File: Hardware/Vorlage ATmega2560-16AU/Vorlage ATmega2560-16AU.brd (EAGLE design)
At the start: 160 x 100 mm, 152 parts, among them IC1 CD74HC14PW, IC2 ATMEGA2560640V-8AU, IC3 SS39E, IC4 SS39E, IC5 74AC138D, IC6 XC6210B332MR, Q1 16MHz, Q10 PMV27UPER, Q2 32.768kHz, Q3 PMV27UPER, Q4 PMV27UPER, Q5 PMV27UPER, Q6 PMV27UPER, Q7 PMV27UPER, Q8 PMV27UPER, Q9 PMV27UPER, U1 LM35DZ, X1 2510-, X2 +5V, X3 2514-, X4 2510-, X5 2510-

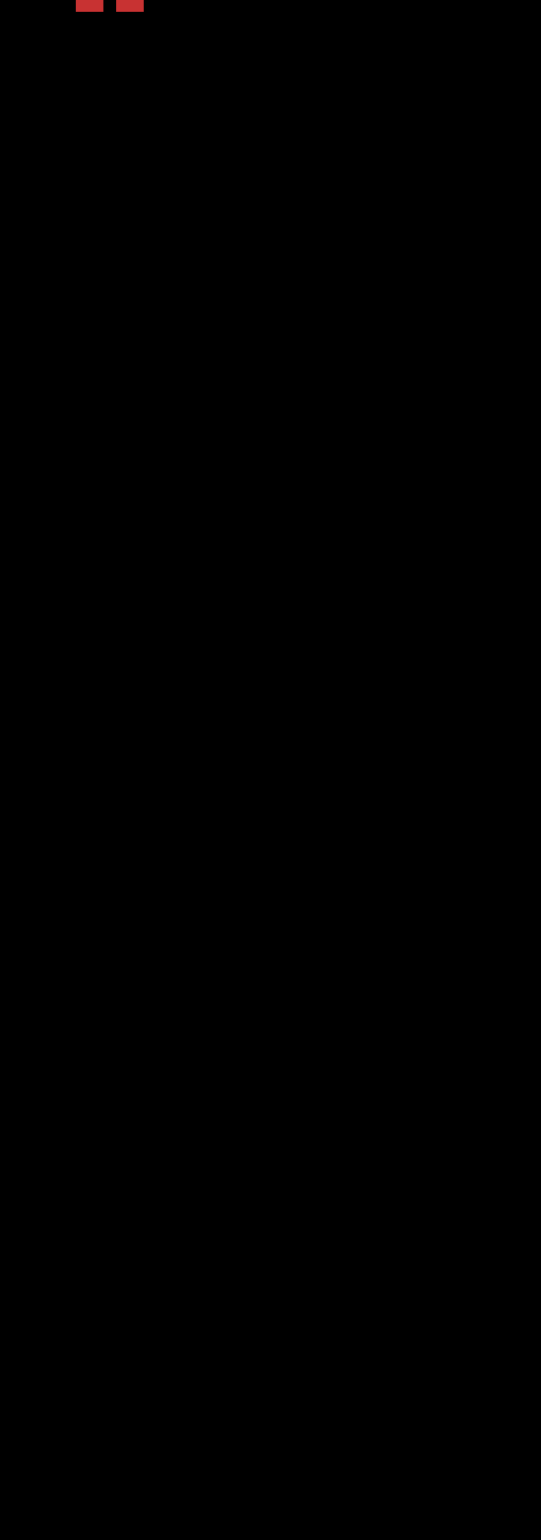
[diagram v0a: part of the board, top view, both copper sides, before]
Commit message: LED Helligkeit mit einstellbarem PWM
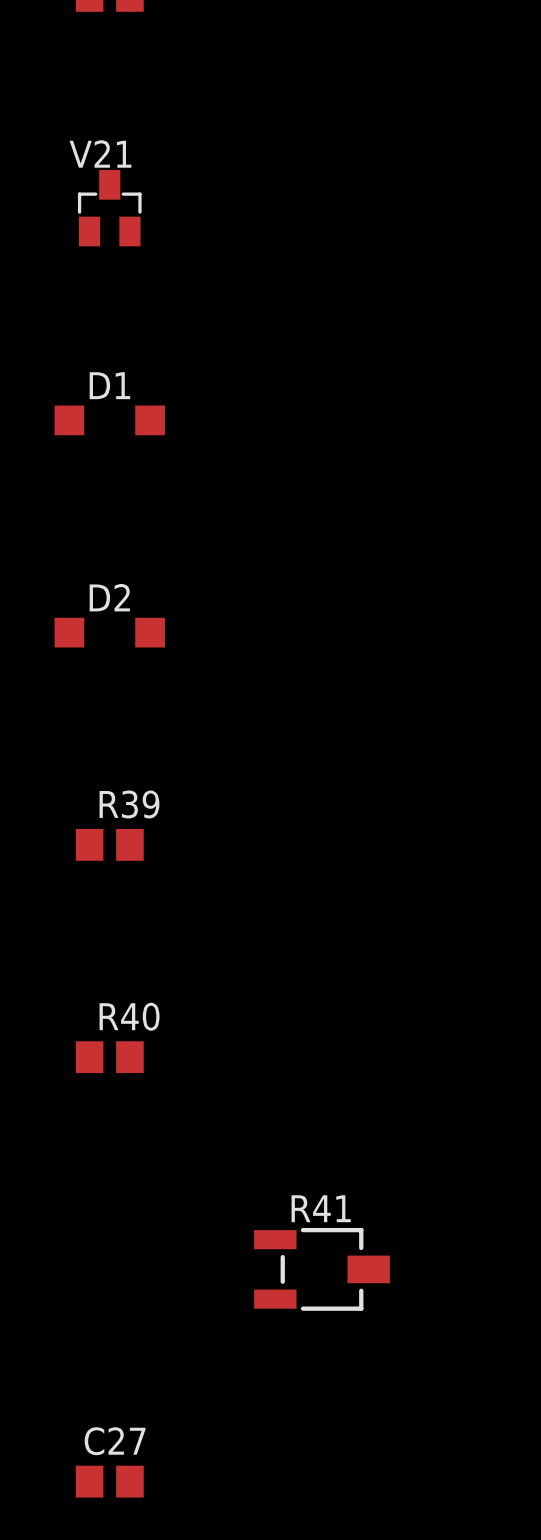
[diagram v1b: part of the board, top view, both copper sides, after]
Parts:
- added C27: 22nF, rcl:C0805
- added D1, D2: (no value), diode:SOD123
- added R39, R40: 470, rcl:R0805
- added R41: 50k, pot:3223G
- added V21: PMV20EN, transistor-fet-mit-BSS138:SOT23
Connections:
- new net LED_GND: +5V-POWER.C, V10.2, V11.2, V12.2, V13.2, V14.2, V15.2, V16.2, V17.2, V18.2, V19.2, V20.2, V21.3, V5.2, V6.2, V7.2, V8.2, V9.2
- new net N$36: D1.C, D2.A, IC1.6, V21.1
- new net N$38: D1.A, R39.1
- new net N$41: D2.C, R40.1
- new net N$42: R39.2, R41.1
- new net N$43: R40.2, R41.3
- new net N$44: C27.1, IC1.5, R41.2
- net GND: now also C27.2, V21.2; no longer +5V-POWER.C, IC1.5, V10.2, V11.2, V12.2, V13.2, V14.2, V15.2, V16.2, V17.2, V18.2, V19.2, V20.2, V5.2, V6.2, V7.2, V8.2, V9.2

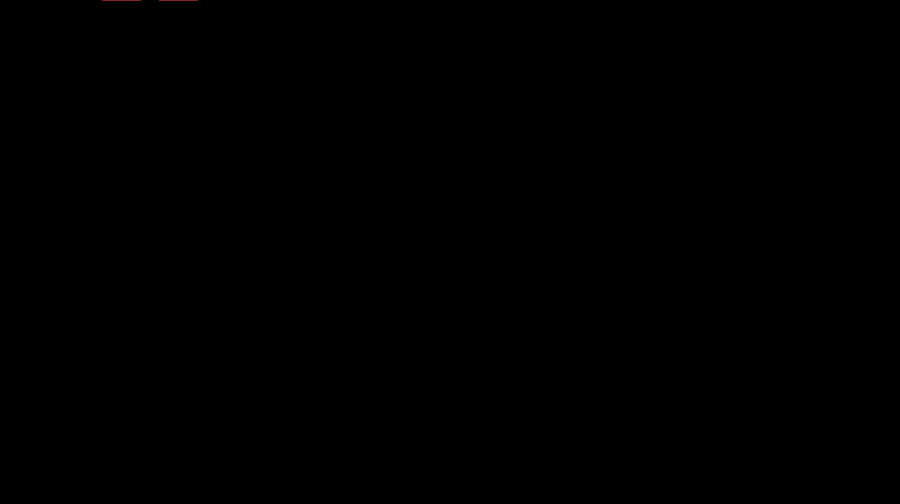
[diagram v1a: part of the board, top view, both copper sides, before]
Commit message: Reset button hinzugefügt
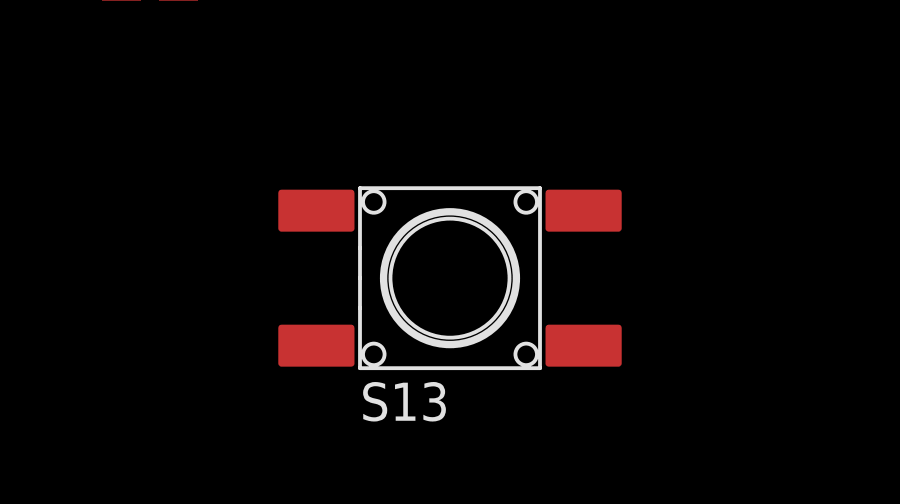
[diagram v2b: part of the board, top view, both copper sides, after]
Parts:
- added S13: (no value), SmartPrj:TS42_4PAD
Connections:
- net GND: now also S13.1, S13.2
- net RESET: now also S13.3, S13.4
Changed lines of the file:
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@@
 <attribute name="VALUE" x="-131.27" y="-382.54" size="1.27" layer="27"/>
+</element>
+<element name="S13" library="SmartPrj" package="TS42_4PAD" value="" x="-120" y="-390" smashed="yes">
+<attribute name="NAME" x="-123" y="-394.754" size="1.27" layer="21"/>
+<attribute name="VALUE" x="-123" y="-386" size="1.27" layer="21"/>
 </element>
 </elements>
@@
 <contactref element="C27" pad="2"/>
 <contactref element="V21" pad="2"/>
+<contactref element="S13" pad="2"/>
+<contactref element="S13" pad="1"/>
 <wire x1="-116.13" y1="-163.92" x2="-114.92" y2="-138.73" width="0" layer="19" extent="1-1"/>
 <wire x1="-119.38" y1="-169.92" x2="-116.13" y2="-163.92" width="0" layer="19" extent="1-1"/>
@@
 <wire x1="-20" y1="-182.54" x2="-22.5" y2="-167" width="0" layer="19" extent="1-1"/>
 <wire x1="-129.05" y1="-380" x2="-129.05" y2="-321.1" width="0" layer="19" extent="1-1"/>
+<wire x1="-124.454" y1="-387.75" x2="-129.05" y2="-380" width="0" layer="19" extent="1-1"/>
+<wire x1="-115.546" y1="-387.75" x2="-124.454" y2="-387.75" width="0" layer="19" extent="1-1"/>
 <wire x1="-110.49" y1="40.6" x2="-114.92" y2="-138.73" width="0" layer="19" extent="1-1"/>
 <wire x1="-109.22" y1="60.92" x2="-110.49" y2="40.6" width="0" layer="19" extent="1-1"/>
@@
 <contactref element="IC2" pad="30"/>
 <contactref element="JTAG" pad="6"/>
+<contactref element="S13" pad="3"/>
+<contactref element="S13" pad="4"/>
+<wire x1="-124.454" y1="-392.25" x2="-115.546" y2="-392.25" width="0" layer="19" extent="1-1"/>
+<wire x1="-62.54" y1="-190" x2="-115.546" y2="-392.25" width="0" layer="19" extent="1-1"/>
 <wire x1="-34.48" y1="30.1" x2="-62.54" y2="-190" width="0" layer="19" extent="1-1"/>
 <wire x1="-127.152" y1="135.89" x2="-34.48" y2="30.1" width="0" layer="19" extent="1-1"/>
